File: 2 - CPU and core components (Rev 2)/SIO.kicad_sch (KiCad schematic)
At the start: 23 parts

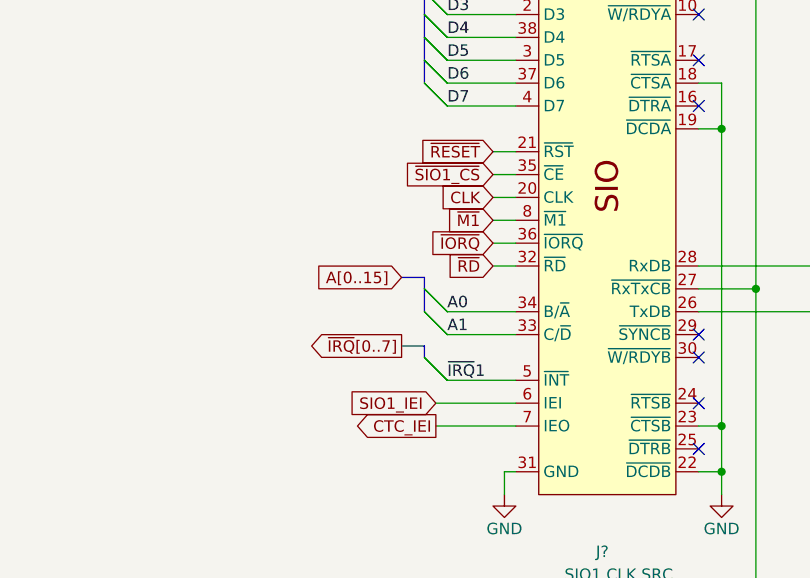
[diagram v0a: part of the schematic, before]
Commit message: Replacing a lot of TTL chips by 2 PLDs. Also, added blinkenlights.
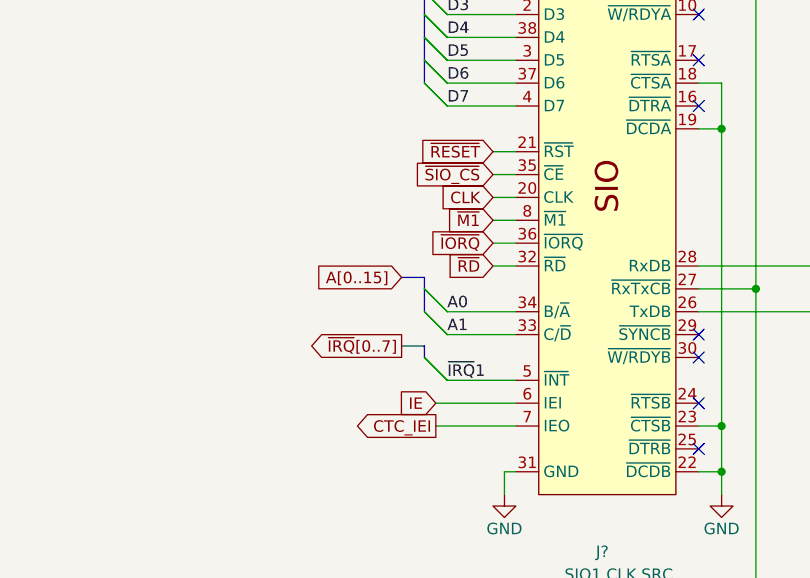
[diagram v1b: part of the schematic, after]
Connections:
- net SIO1_IEI renamed IE
- net ~{SIO1_CS} renamed ~{SIO_CS}
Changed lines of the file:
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@@
     )
   )
-  (global_label "~{SIO1_CS}" (shape input) (at 102.87 82.55 180) (fields_autoplaced)
+  (global_label "~{SIO_CS}" (shape input) (at 102.87 82.55 180) (fields_autoplaced)
     (effects (font (size 1.27 1.27)) (justify right))
-    (property "Intersheetrefs" "${INTERSHEET_REFS}" (at 92.0834 82.55 0)
+    (property "Intersheetrefs" "${INTERSHEET_REFS}" (at 93.2929 82.55 0)
       (effects (font (size 1.27 1.27)) (justify right) hide)
     )
@@
     )
   )
-  (global_label "SIO1_IEI" (shape input) (at 96.52 107.95 180) (fields_autoplaced)
+  (global_label "IE" (shape input) (at 96.52 107.95 180) (fields_autoplaced)
     (effects (font (size 1.27 1.27)) (justify right))
-    (property "Intersheetrefs" "${INTERSHEET_REFS}" (at 85.8543 107.95 0)
+    (property "Intersheetrefs" "${INTERSHEET_REFS}" (at 91.781 107.95 0)
       (effects (font (size 1.27 1.27)) (justify right) hide)
     )
@@
       (project "2 - CPU and core components (Rev 2)"
         (path "/fc5c05aa-044e-4225-a29e-03b20eedf682/494e1a83-34fd-4d1b-916c-a62092caa423"
-          (reference "C14") (unit 1)
+          (reference "C15") (unit 1)
         )
       )
@@
       (project "2 - CPU and core components (Rev 2)"
         (path "/fc5c05aa-044e-4225-a29e-03b20eedf682/494e1a83-34fd-4d1b-916c-a62092caa423"
-          (reference "#PWR071") (unit 1)
+          (reference "#PWR075") (unit 1)
         )
       )
@@
       (project "2 - CPU and core components (Rev 2)"
         (path "/fc5c05aa-044e-4225-a29e-03b20eedf682/494e1a83-34fd-4d1b-916c-a62092caa423"
-          (reference "#PWR056") (unit 1)
+          (reference "#PWR060") (unit 1)
         )
       )
@@
       (project "2 - CPU and core components (Rev 2)"
         (path "/fc5c05aa-044e-4225-a29e-03b20eedf682/494e1a83-34fd-4d1b-916c-a62092caa423"
-          (reference "U13") (unit 1)
+          (reference "U15") (unit 1)
         )
       )
@@
       (project "2 - CPU and core components (Rev 2)"
         (path "/fc5c05aa-044e-4225-a29e-03b20eedf682/494e1a83-34fd-4d1b-916c-a62092caa423"
-          (reference "D2") (unit 1)
+          (reference "D4") (unit 1)
         )
       )
@@
       (project "2 - CPU and core components (Rev 2)"
         (path "/fc5c05aa-044e-4225-a29e-03b20eedf682/494e1a83-34fd-4d1b-916c-a62092caa423"
-          (reference "D5") (unit 1)
+          (reference "D7") (unit 1)
         )
       )
@@
       (project "2 - CPU and core components (Rev 2)"
         (path "/fc5c05aa-044e-4225-a29e-03b20eedf682/494e1a83-34fd-4d1b-916c-a62092caa423"
-          (reference "#PWR069") (unit 1)
+          (reference "#PWR073") (unit 1)
         )
       )
@@
       (project "2 - CPU and core components (Rev 2)"
         (path "/fc5c05aa-044e-4225-a29e-03b20eedf682/494e1a83-34fd-4d1b-916c-a62092caa423"
-          (reference "U14") (unit 1)
+          (reference "U16") (unit 1)
         )
       )
@@
       (project "2 - CPU and core components (Rev 2)"
         (path "/fc5c05aa-044e-4225-a29e-03b20eedf682/494e1a83-34fd-4d1b-916c-a62092caa423"
-          (reference "#PWR064") (unit 1)
+          (reference "#PWR068") (unit 1)
         )
       )
@@
       (project "2 - CPU and core components (Rev 2)"
         (path "/fc5c05aa-044e-4225-a29e-03b20eedf682/494e1a83-34fd-4d1b-916c-a62092caa423"
-          (reference "D1") (unit 1)
+          (reference "D3") (unit 1)
         )
       )
@@
       (project "2 - CPU and core components (Rev 2)"
         (path "/fc5c05aa-044e-4225-a29e-03b20eedf682/494e1a83-34fd-4d1b-916c-a62092caa423"
-          (reference "C15") (unit 1)
+          (reference "C16") (unit 1)
         )
       )
@@
       (project "2 - CPU and core components (Rev 2)"
         (path "/fc5c05aa-044e-4225-a29e-03b20eedf682/494e1a83-34fd-4d1b-916c-a62092caa423"
-          (reference "D4") (unit 1)
+          (reference "D6") (unit 1)
         )
       )
@@
       (project "2 - CPU and core components (Rev 2)"
         (path "/fc5c05aa-044e-4225-a29e-03b20eedf682/494e1a83-34fd-4d1b-916c-a62092caa423"
-          (reference "#PWR057") (unit 1)
+          (reference "#PWR061") (unit 1)
         )
       )
@@
       (project "2 - CPU and core components (Rev 2)"
         (path "/fc5c05aa-044e-4225-a29e-03b20eedf682/494e1a83-34fd-4d1b-916c-a62092caa423"
-          (reference "C18") (unit 1)
+          (reference "C19") (unit 1)
         )
       )
@@
       (project "2 - CPU and core components (Rev 2)"
         (path "/fc5c05aa-044e-4225-a29e-03b20eedf682/494e1a83-34fd-4d1b-916c-a62092caa423"
-          (reference "C16") (unit 1)
+          (reference "C17") (unit 1)
         )
       )
@@
       (project "2 - CPU and core components (Rev 2)"
         (path "/fc5c05aa-044e-4225-a29e-03b20eedf682/494e1a83-34fd-4d1b-916c-a62092caa423"
-          (reference "#PWR065") (unit 1)
+          (reference "#PWR069") (unit 1)
         )
       )
@@
       (project "2 - CPU and core components (Rev 2)"
         (path "/fc5c05aa-044e-4225-a29e-03b20eedf682/494e1a83-34fd-4d1b-916c-a62092caa423"
-          (reference "#PWR072") (unit 1)
+          (reference "#PWR076") (unit 1)
         )
       )
@@
       (project "2 - CPU and core components (Rev 2)"
         (path "/fc5c05aa-044e-4225-a29e-03b20eedf682/494e1a83-34fd-4d1b-916c-a62092caa423"
-          (reference "D3") (unit 1)
+          (reference "D5") (unit 1)
         )
       )
@@
       (project "2 - CPU and core components (Rev 2)"
         (path "/fc5c05aa-044e-4225-a29e-03b20eedf682/494e1a83-34fd-4d1b-916c-a62092caa423"
-          (reference "#PWR067") (unit 1)
+          (reference "#PWR071") (unit 1)
         )
       )
@@
       (project "2 - CPU and core components (Rev 2)"
         (path "/fc5c05aa-044e-4225-a29e-03b20eedf682/494e1a83-34fd-4d1b-916c-a62092caa423"
-          (reference "#PWR068") (unit 1)
+          (reference "#PWR072") (unit 1)
         )
       )
@@
       (project "2 - CPU and core components (Rev 2)"
         (path "/fc5c05aa-044e-4225-a29e-03b20eedf682/494e1a83-34fd-4d1b-916c-a62092caa423"
-          (reference "#PWR060") (unit 1)
+          (reference "#PWR064") (unit 1)
         )
       )
@@
       (project "2 - CPU and core components (Rev 2)"
         (path "/fc5c05aa-044e-4225-a29e-03b20eedf682/494e1a83-34fd-4d1b-916c-a62092caa423"
-          (reference "#PWR058") (unit 1)
+          (reference "#PWR062") (unit 1)
         )
       )
@@
       (project "2 - CPU and core components (Rev 2)"
         (path "/fc5c05aa-044e-4225-a29e-03b20eedf682/494e1a83-34fd-4d1b-916c-a62092caa423"
-          (reference "#PWR066") (unit 1)
+          (reference "#PWR070") (unit 1)
         )
       )
@@
       (project "2 - CPU and core components (Rev 2)"
         (path "/fc5c05aa-044e-4225-a29e-03b20eedf682/494e1a83-34fd-4d1b-916c-a62092caa423"
-          (reference "D6") (unit 1)
+          (reference "D8") (unit 1)
         )
       )
@@
       (project "2 - CPU and core components (Rev 2)"
         (path "/fc5c05aa-044e-4225-a29e-03b20eedf682/494e1a83-34fd-4d1b-916c-a62092caa423"
-          (reference "#PWR070") (unit 1)
+          (reference "#PWR074") (unit 1)
         )
       )
@@
       (project "2 - CPU and core components (Rev 2)"
         (path "/fc5c05aa-044e-4225-a29e-03b20eedf682/494e1a83-34fd-4d1b-916c-a62092caa423"
-          (reference "#PWR061") (unit 1)
+          (reference "#PWR065") (unit 1)
         )
       )
@@
       (project "2 - CPU and core components (Rev 2)"
         (path "/fc5c05aa-044e-4225-a29e-03b20eedf682/494e1a83-34fd-4d1b-916c-a62092caa423"
-          (reference "#PWR062") (unit 1)
+          (reference "#PWR066") (unit 1)
         )
       )
@@
       (project "2 - CPU and core components (Rev 2)"
         (path "/fc5c05aa-044e-4225-a29e-03b20eedf682/494e1a83-34fd-4d1b-916c-a62092caa423"
-          (reference "#PWR063") (unit 1)
+          (reference "#PWR067") (unit 1)
         )
       )
@@
       (project "2 - CPU and core components (Rev 2)"
         (path "/fc5c05aa-044e-4225-a29e-03b20eedf682/494e1a83-34fd-4d1b-916c-a62092caa423"
-          (reference "C17") (unit 1)
+          (reference "C18") (unit 1)
         )
       )
@@
       (project "2 - CPU and core components (Rev 2)"
         (path "/fc5c05aa-044e-4225-a29e-03b20eedf682/494e1a83-34fd-4d1b-916c-a62092caa423"
-          (reference "U12") (unit 1)
+          (reference "U14") (unit 1)
         )
       )
@@
       (project "2 - CPU and core components (Rev 2)"
         (path "/fc5c05aa-044e-4225-a29e-03b20eedf682/494e1a83-34fd-4d1b-916c-a62092caa423"
-          (reference "#PWR059") (unit 1)
-        )
-      )
+          (reference "#PWR063") (unit 1)
+        )
+      )

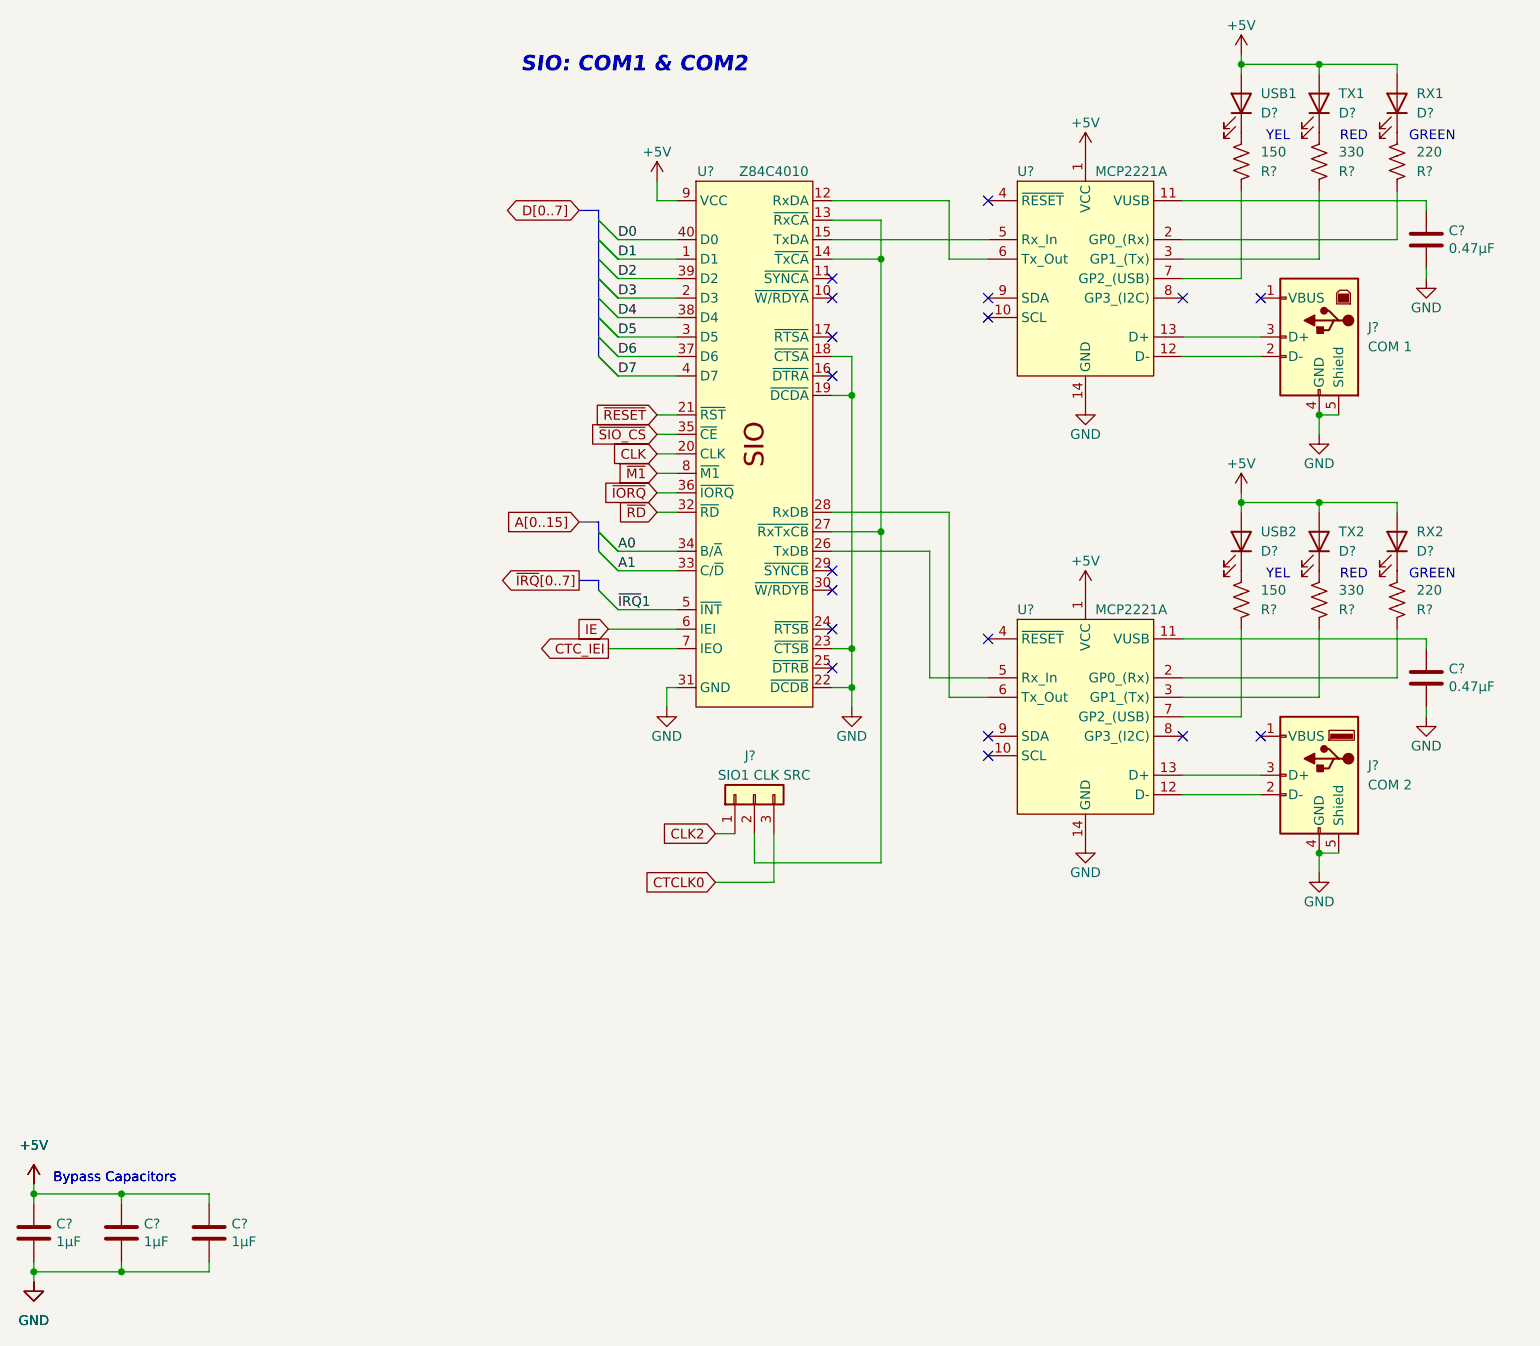
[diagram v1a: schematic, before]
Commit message: Added Interrupt Enable daisy chain jumpers between the ISA slots
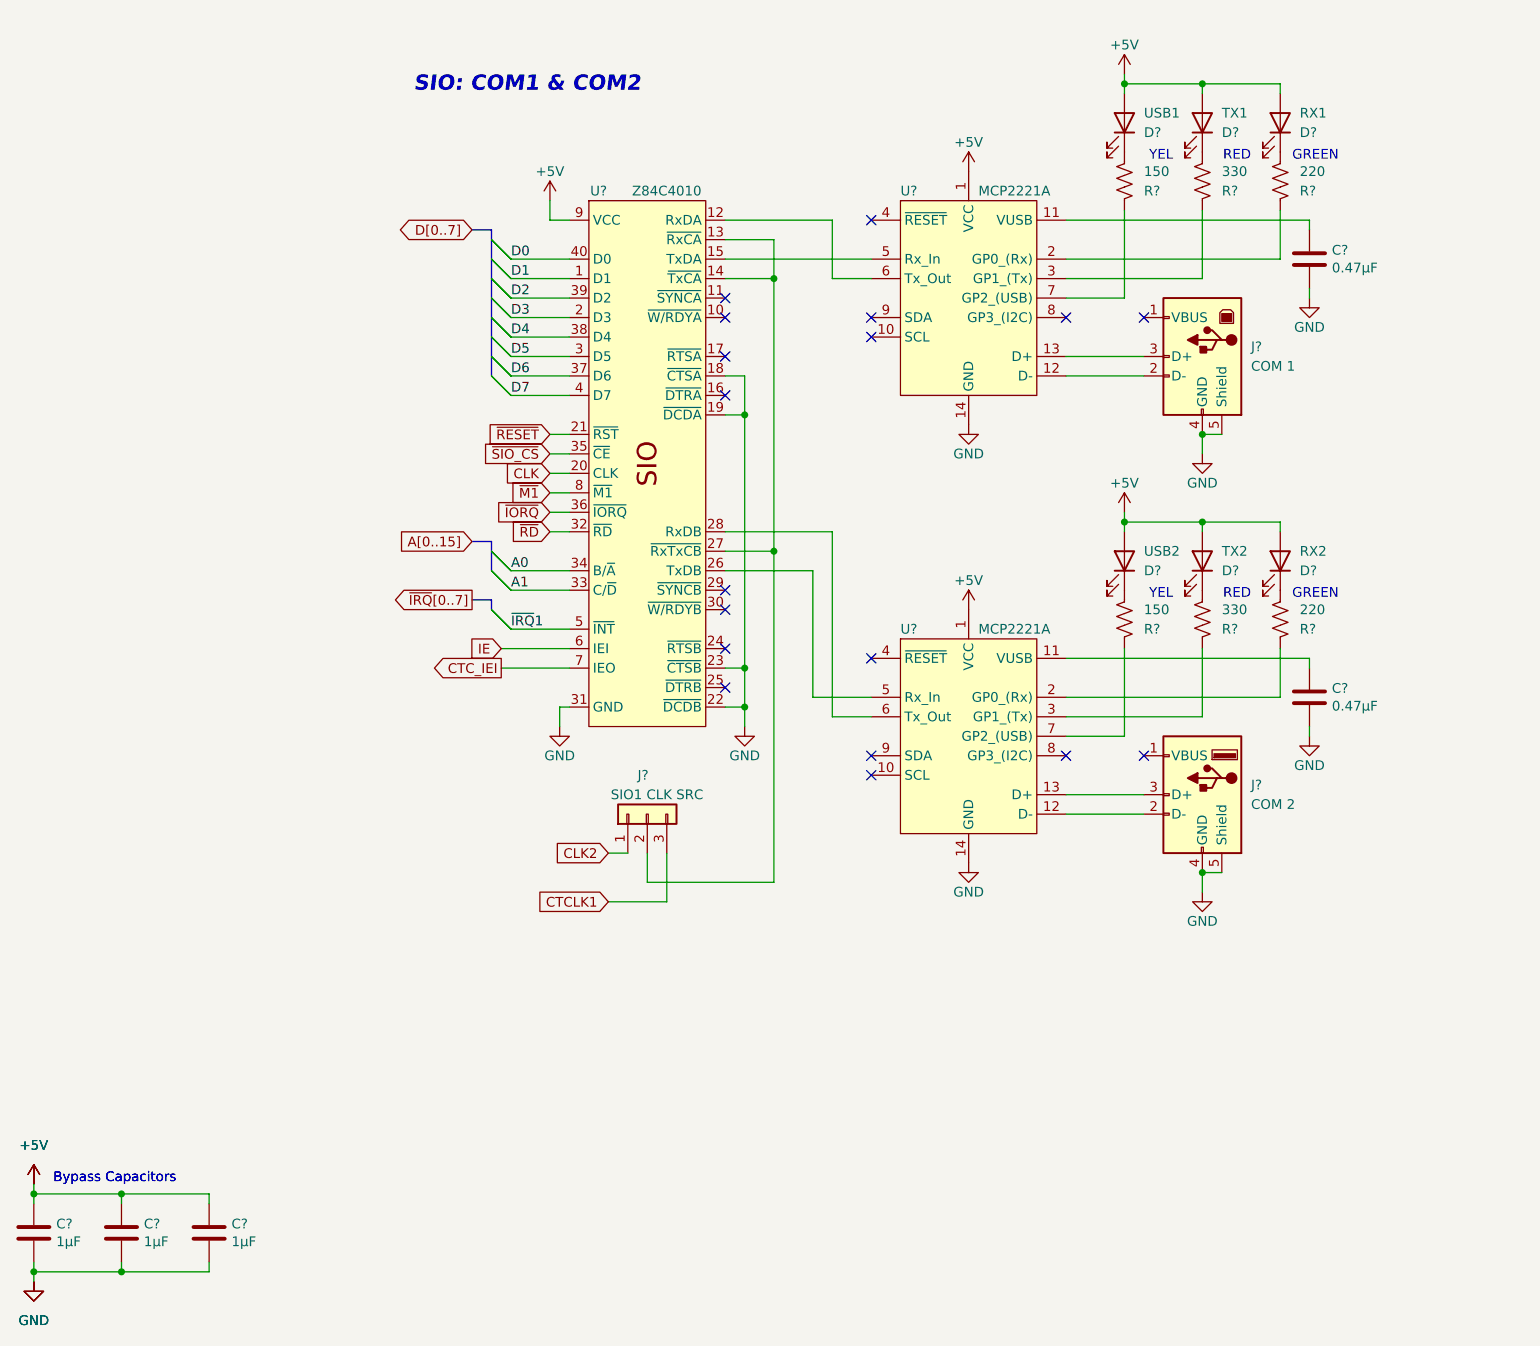
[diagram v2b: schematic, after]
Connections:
- net CTCLK0 renamed CTCLK1
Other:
- moved on the sheet: C?, D?, J?, R?, U?

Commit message: Finished component placement, currently routing.
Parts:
- added D?: DTRB, LED_THT:LED_D3.0mm_Horizontal_O1.27mm_Z2.0mm_Clear, symbol Device:LED
- added D?: DTRA, LED_THT:LED_D3.0mm_Horizontal_O1.27mm_Z2.0mm_Clear, symbol Device:LED
- added U1: 74HCT132, Package_DIP:DIP-14_W7.62mm_Socket, symbol 74xx:74LS132
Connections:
- net +5V: now also R?.2, R?.2, R?.2, R?.2, R?.2, R?.2; no longer D?.2 (A), D?.2 (A), D?.2 (A), D?.2 (A), D?.2 (A), D?.2 (A)
- net at R?.1: now also D?.2 (A); no longer U?.2 (GP0_(Rx))
- net at D?.1 (K): now also U?.2 (GP0_(Rx)); no longer R?.2
- net D1-: now reaches J?.2 (D-), U?.12 (D-)
- net D1+: now reaches J?.3 (D+), U?.13 (D+)
- net at U?.3 (GP1_(Tx)): now also D?.1 (K); no longer R?.1 (x2)
- net at U?.7 (GP2_(USB)): now also D?.1 (K); no longer R?.1
- net at D?.1 (K): now also U?.7 (GP2_(USB)); no longer R?.2
- net D2-: now reaches J?.2 (D-), U?.12 (D-)
- net D2+: now reaches J?.3 (D+), U?.13 (D+)
- net at U?.2 (GP0_(Rx)): now also D?.1 (K); no longer R?.1
- net at R?.1: now also D?.2 (A); no longer U?.7 (GP2_(USB))
- net at U?.16 (~{DTRA}): now also U1.10, U1.9
- net at U?.25 (~{DTRB}): now also U1.12, U1.13
- new net: D?.1 (K), U1.11
- new net: D?.1 (K), U1.8
- new net: D?.2 (A), R?.1 (x4)
- new net R_FTRA: D?.2 (A)
- new net R_FTRB: D?.2 (A)
- no-connect marks 18 -> 16
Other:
- moved on the sheet: C?, D?, J?, R?, U?
